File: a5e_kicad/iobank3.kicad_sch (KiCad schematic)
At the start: 3 parts, among them U7 A5EB013B-B23B

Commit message: add escape routing for channel A lpddr
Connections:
- net dq0: now also U7.M65 (3A_B_IO15_IOB_DIFF_IO_3A_B17n); no longer U7.AB62 (3A_B_IO12_IOB_DIFF_IO_3A_B18p)
- net dq1: now also U7.T51 (3A_B_IO22_IOB_DIFF_IO_3A_B13p); no longer U7.W62 (3A_B_IO13_IOB_DIFF_IO_3A_B18n)
- net dq5: now also U7.AB62 (3A_B_IO12_IOB_DIFF_IO_3A_B18p); no longer U7.M65 (3A_B_IO15_IOB_DIFF_IO_3A_B17n)
- net dq6: now also U7.W62 (3A_B_IO13_IOB_DIFF_IO_3A_B18n); no longer U7.T51 (3A_B_IO22_IOB_DIFF_IO_3A_B13p)
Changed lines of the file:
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@@
 		)
 	)
-	(label "dq6"
+	(label "dq1"
 		(at 208.28 104.14 0)
 		(effects
@@
 		)
 	)
-	(label "dq0"
+	(label "dq5"
 		(at 208.28 129.54 0)
 		(effects
@@
 		)
 	)
-	(label "dq5"
+	(label "dq0"
 		(at 208.28 121.92 0)
 		(effects
@@
 		)
 	)
-	(label "dq1"
+	(label "dq6"
 		(at 208.28 127 0)
 		(effects

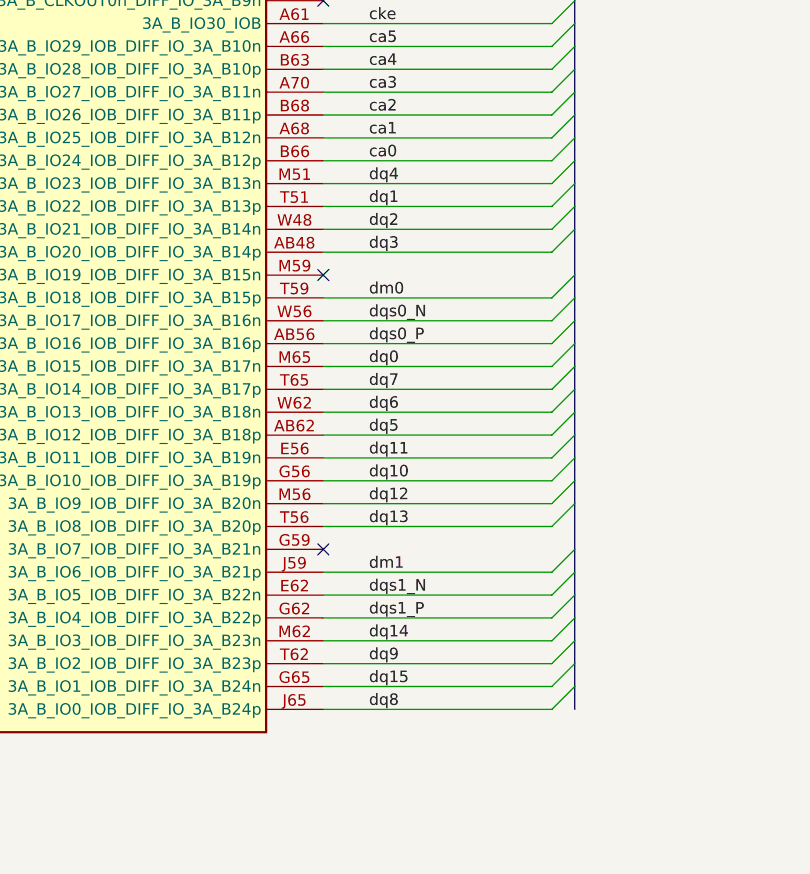
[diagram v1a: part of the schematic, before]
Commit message: iobank3: swap the channel A bytes (BL0 = byte 0, BL1 = byte 1)
Relabel the 22 U7-side labels of dq0-15, dqs0/1, dm0/1; each net keeps its
lane-pin position. Netlist: only the 22 channel A U7<->U12 pairs change.
BYTE_SWIZZLE_CH0=0 1 X X X X 3 2, PIN_SWIZZLE_CH0_DQS0=5 6 7 0 3 2 1 4
(DQS1-3 unchanged). The PCB is not updated yet: the routed dqs0/1 and dm0/1
on In2 end on the other byte's balls and need rerouting. In-lane pin swaps
follow by hand while routing.
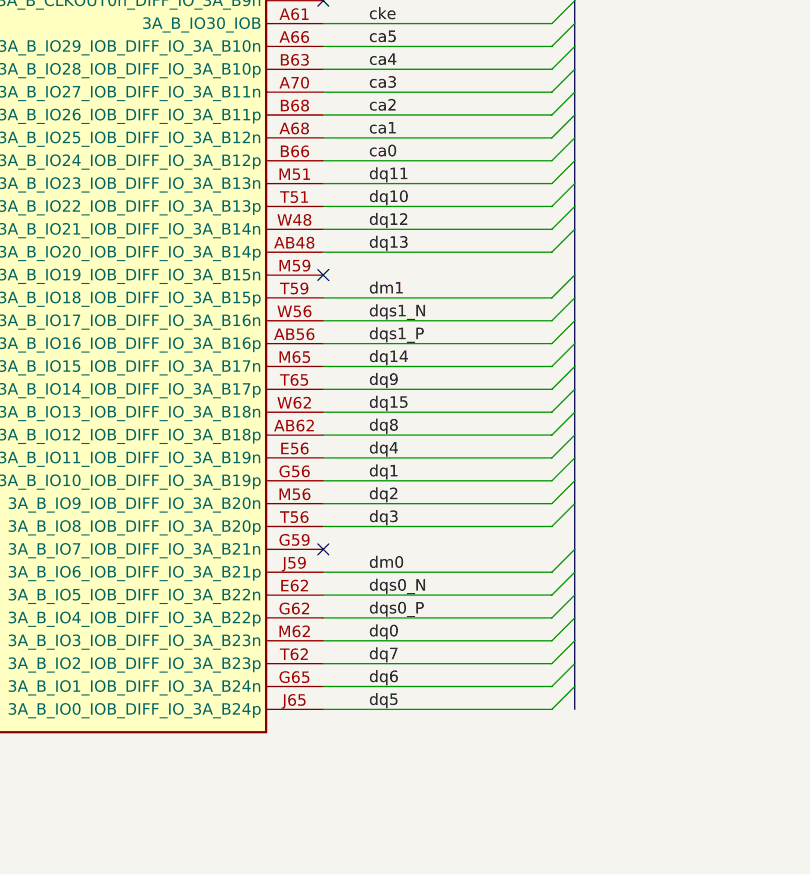
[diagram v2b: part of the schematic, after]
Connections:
- net dm0: now also U7.J59 (3A_B_IO6_IOB_DIFF_IO_3A_B21p); no longer U7.T59 (3A_B_IO18_IOB_DIFF_IO_3A_B15p)
- net dm1: now also U7.T59 (3A_B_IO18_IOB_DIFF_IO_3A_B15p); no longer U7.J59 (3A_B_IO6_IOB_DIFF_IO_3A_B21p)
- net dq0: now also U7.M62 (3A_B_IO3_IOB_DIFF_IO_3A_B23n); no longer U7.M65 (3A_B_IO15_IOB_DIFF_IO_3A_B17n)
- net dq1: now also U7.G56 (3A_B_IO10_IOB_DIFF_IO_3A_B19p); no longer U7.T51 (3A_B_IO22_IOB_DIFF_IO_3A_B13p)
- net dq10: now also U7.T51 (3A_B_IO22_IOB_DIFF_IO_3A_B13p); no longer U7.G56 (3A_B_IO10_IOB_DIFF_IO_3A_B19p)
- net dq11: now also U7.M51 (3A_B_IO23_IOB_DIFF_IO_3A_B13n); no longer U7.E56 (3A_B_IO11_IOB_DIFF_IO_3A_B19n)
- net dq12: now also U7.W48 (3A_B_IO21_IOB_DIFF_IO_3A_B14n); no longer U7.M56 (3A_B_IO9_IOB_DIFF_IO_3A_B20n)
- net dq13: now also U7.AB48 (3A_B_IO20_IOB_DIFF_IO_3A_B14p); no longer U7.T56 (3A_B_IO8_IOB_DIFF_IO_3A_B20p)
- net dq14: now also U7.M65 (3A_B_IO15_IOB_DIFF_IO_3A_B17n); no longer U7.M62 (3A_B_IO3_IOB_DIFF_IO_3A_B23n)
- net dq15: now also U7.W62 (3A_B_IO13_IOB_DIFF_IO_3A_B18n); no longer U7.G65 (3A_B_IO1_IOB_DIFF_IO_3A_B24n)
- net dq2: now also U7.M56 (3A_B_IO9_IOB_DIFF_IO_3A_B20n); no longer U7.W48 (3A_B_IO21_IOB_DIFF_IO_3A_B14n)
- net dq3: now also U7.T56 (3A_B_IO8_IOB_DIFF_IO_3A_B20p); no longer U7.AB48 (3A_B_IO20_IOB_DIFF_IO_3A_B14p)
- net dq4: now also U7.E56 (3A_B_IO11_IOB_DIFF_IO_3A_B19n); no longer U7.M51 (3A_B_IO23_IOB_DIFF_IO_3A_B13n)
- net dq5: now also U7.J65 (3A_B_IO0_IOB_DIFF_IO_3A_B24p); no longer U7.AB62 (3A_B_IO12_IOB_DIFF_IO_3A_B18p)
- net dq6: now also U7.G65 (3A_B_IO1_IOB_DIFF_IO_3A_B24n); no longer U7.W62 (3A_B_IO13_IOB_DIFF_IO_3A_B18n)
- net dq7: now also U7.T62 (3A_B_IO2_IOB_DIFF_IO_3A_B23p); no longer U7.T65 (3A_B_IO14_IOB_DIFF_IO_3A_B17p)
- net dq8: now also U7.AB62 (3A_B_IO12_IOB_DIFF_IO_3A_B18p); no longer U7.J65 (3A_B_IO0_IOB_DIFF_IO_3A_B24p)
- net dq9: now also U7.T65 (3A_B_IO14_IOB_DIFF_IO_3A_B17p); no longer U7.T62 (3A_B_IO2_IOB_DIFF_IO_3A_B23p)
- net dqs0_N: now also U7.E62 (3A_B_IO5_IOB_DIFF_IO_3A_B22n); no longer U7.W56 (3A_B_IO17_IOB_DIFF_IO_3A_B16n)
- net dqs0_P: now also U7.G62 (3A_B_IO4_IOB_DIFF_IO_3A_B22p); no longer U7.AB56 (3A_B_IO16_IOB_DIFF_IO_3A_B16p)
- net dqs1_N: now also U7.W56 (3A_B_IO17_IOB_DIFF_IO_3A_B16n); no longer U7.E62 (3A_B_IO5_IOB_DIFF_IO_3A_B22n)
- net dqs1_P: now also U7.AB56 (3A_B_IO16_IOB_DIFF_IO_3A_B16p); no longer U7.G62 (3A_B_IO4_IOB_DIFF_IO_3A_B22p)
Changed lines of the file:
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@@
 		)
 	)
-	(label "dqs0_N"
+	(label "dqs1_N"
 		(at 208.28 116.84 0)
 		(effects
@@
 		)
 	)
-	(label "dq7"
+	(label "dq9"
 		(at 208.28 124.46 0)
 		(effects
@@
 		)
 	)
-	(label "dq1"
+	(label "dq10"
 		(at 208.28 104.14 0)
 		(effects
@@
 		)
 	)
-	(label "dq5"
+	(label "dq8"
 		(at 208.28 129.54 0)
 		(effects
@@
 		)
 	)
-	(label "dm1"
+	(label "dm0"
 		(at 208.28 144.78 0)
 		(effects
@@
 		)
 	)
-	(label "dq12"
+	(label "dq2"
 		(at 208.28 137.16 0)
 		(effects
@@
 		)
 	)
-	(label "dq3"
+	(label "dq13"
 		(at 208.28 109.22 0)
 		(effects
@@
 		)
 	)
-	(label "dq8"
+	(label "dq5"
 		(at 208.28 160.02 0)
 		(effects
@@
 		)
 	)
+	(label "dq4"
+		(at 208.28 132.08 0)
+		(effects
+			(font
+				(size 1.27 1.27)
+			)
+			(justify left bottom)
+		)
+	)
 	(label "dq11"
-		(at 208.28 132.08 0)
-		(effects
-			(font
-				(size 1.27 1.27)
-			)
-			(justify left bottom)
-		)
-	)
-	(label "dq4"
 		(at 208.28 101.6 0)
 		(effects
@@
 		)
 	)
-	(label "dq9"
+	(label "dq7"
 		(at 208.28 154.94 0)
 		(effects
@@
 		)
 	)
-	(label "dqs1_P"
+	(label "dqs0_P"
 		(at 208.28 149.86 0)
 		(effects
@@
 		)
 	)
-	(label "dq15"
+	(label "dq6"
 		(at 208.28 157.48 0)
 		(effects
@@
 		)
 	)
-	(label "dq14"
+	(label "dq0"
 		(at 208.28 152.4 0)
 		(effects
@@
 		)
 	)
-	(label "dq0"
+	(label "dq14"
 		(at 208.28 121.92 0)
 		(effects
@@
 		)
 	)
-	(label "dq13"
+	(label "dq3"
 		(at 208.28 139.7 0)
 		(effects
@@
 		)
 	)
-	(label "dq10"
+	(label "dq1"
 		(at 208.28 134.62 0)
 		(effects
@@
 		)
 	)
-	(label "dm0"
+	(label "dm1"
 		(at 208.28 114.3 0)
 		(effects
@@
 		)
 	)
-	(label "dqs0_P"
+	(label "dqs1_P"
 		(at 208.28 119.38 0)
 		(effects
@@
 		)
 	)
-	(label "dq2"
+	(label "dq12"
 		(at 208.28 106.68 0)
 		(effects
@@
 		)
 	)
-	(label "dq6"
+	(label "dq15"
 		(at 208.28 127 0)
 		(effects
@@
 		)
 	)
-	(label "dqs1_N"
+	(label "dqs0_N"
 		(at 208.28 147.32 0)
 		(effects

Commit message: route lpddr4 io
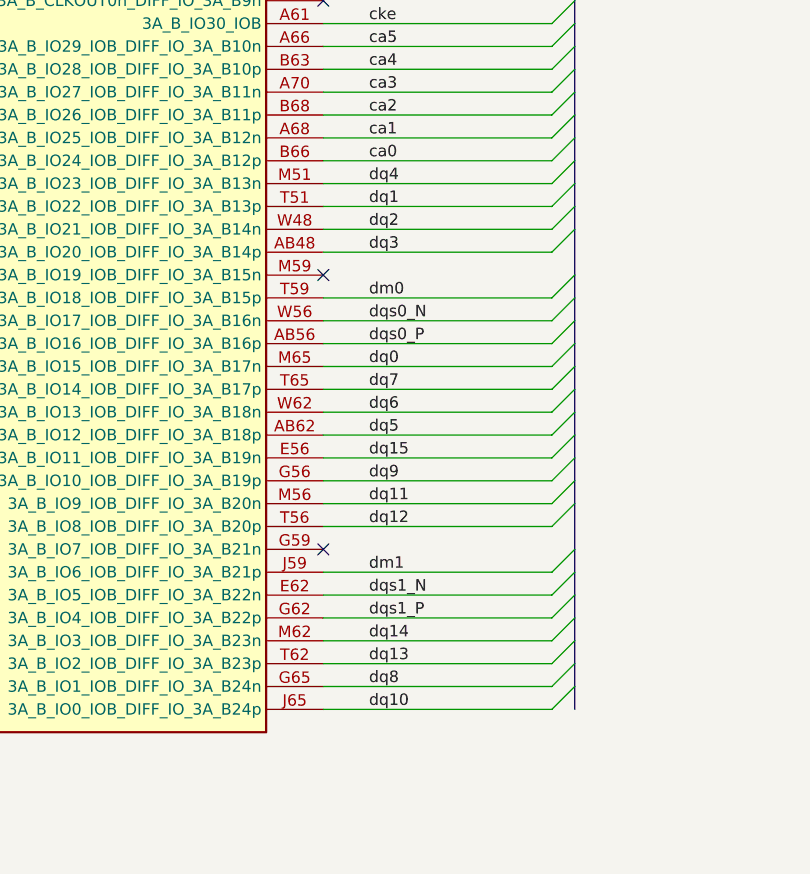
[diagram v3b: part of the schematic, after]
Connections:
- net dm0: now also U7.T59 (3A_B_IO18_IOB_DIFF_IO_3A_B15p); no longer U7.J59 (3A_B_IO6_IOB_DIFF_IO_3A_B21p)
- net dm1: now also U7.J59 (3A_B_IO6_IOB_DIFF_IO_3A_B21p); no longer U7.T59 (3A_B_IO18_IOB_DIFF_IO_3A_B15p)
- net dq0: now also U7.M65 (3A_B_IO15_IOB_DIFF_IO_3A_B17n); no longer U7.M62 (3A_B_IO3_IOB_DIFF_IO_3A_B23n)
- net dq1: now also U7.T51 (3A_B_IO22_IOB_DIFF_IO_3A_B13p); no longer U7.G56 (3A_B_IO10_IOB_DIFF_IO_3A_B19p)
- net dq10: now also U7.J65 (3A_B_IO0_IOB_DIFF_IO_3A_B24p); no longer U7.T51 (3A_B_IO22_IOB_DIFF_IO_3A_B13p)
- net dq11: now also U7.M56 (3A_B_IO9_IOB_DIFF_IO_3A_B20n); no longer U7.M51 (3A_B_IO23_IOB_DIFF_IO_3A_B13n)
- net dq12: now also U7.T56 (3A_B_IO8_IOB_DIFF_IO_3A_B20p); no longer U7.W48 (3A_B_IO21_IOB_DIFF_IO_3A_B14n)
- net dq13: now also U7.T62 (3A_B_IO2_IOB_DIFF_IO_3A_B23p); no longer U7.AB48 (3A_B_IO20_IOB_DIFF_IO_3A_B14p)
- net dq14: now also U7.M62 (3A_B_IO3_IOB_DIFF_IO_3A_B23n); no longer U7.M65 (3A_B_IO15_IOB_DIFF_IO_3A_B17n)
- net dq15: now also U7.E56 (3A_B_IO11_IOB_DIFF_IO_3A_B19n); no longer U7.W62 (3A_B_IO13_IOB_DIFF_IO_3A_B18n)
- net dq2: now also U7.W48 (3A_B_IO21_IOB_DIFF_IO_3A_B14n); no longer U7.M56 (3A_B_IO9_IOB_DIFF_IO_3A_B20n)
- net dq3: now also U7.AB48 (3A_B_IO20_IOB_DIFF_IO_3A_B14p); no longer U7.T56 (3A_B_IO8_IOB_DIFF_IO_3A_B20p)
- net dq4: now also U7.M51 (3A_B_IO23_IOB_DIFF_IO_3A_B13n); no longer U7.E56 (3A_B_IO11_IOB_DIFF_IO_3A_B19n)
- net dq5: now also U7.AB62 (3A_B_IO12_IOB_DIFF_IO_3A_B18p); no longer U7.J65 (3A_B_IO0_IOB_DIFF_IO_3A_B24p)
- net dq6: now also U7.W62 (3A_B_IO13_IOB_DIFF_IO_3A_B18n); no longer U7.G65 (3A_B_IO1_IOB_DIFF_IO_3A_B24n)
- net dq7: now also U7.T65 (3A_B_IO14_IOB_DIFF_IO_3A_B17p); no longer U7.T62 (3A_B_IO2_IOB_DIFF_IO_3A_B23p)
- net dq8: now also U7.G65 (3A_B_IO1_IOB_DIFF_IO_3A_B24n); no longer U7.AB62 (3A_B_IO12_IOB_DIFF_IO_3A_B18p)
- net dq9: now also U7.G56 (3A_B_IO10_IOB_DIFF_IO_3A_B19p); no longer U7.T65 (3A_B_IO14_IOB_DIFF_IO_3A_B17p)
- net dqs0_N: now also U7.W56 (3A_B_IO17_IOB_DIFF_IO_3A_B16n); no longer U7.E62 (3A_B_IO5_IOB_DIFF_IO_3A_B22n)
- net dqs0_P: now also U7.AB56 (3A_B_IO16_IOB_DIFF_IO_3A_B16p); no longer U7.G62 (3A_B_IO4_IOB_DIFF_IO_3A_B22p)
- net dqs1_N: now also U7.E62 (3A_B_IO5_IOB_DIFF_IO_3A_B22n); no longer U7.W56 (3A_B_IO17_IOB_DIFF_IO_3A_B16n)
- net dqs1_P: now also U7.G62 (3A_B_IO4_IOB_DIFF_IO_3A_B22p); no longer U7.AB56 (3A_B_IO16_IOB_DIFF_IO_3A_B16p)
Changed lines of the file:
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@@
 		)
 	)
-	(label "dqs1_N"
+	(label "dqs0_N"
 		(at 208.28 116.84 0)
 		(effects
@@
 		)
 	)
-	(label "dq9"
+	(label "dq7"
 		(at 208.28 124.46 0)
 		(effects
@@
 		)
 	)
-	(label "dq10"
+	(label "dq1"
 		(at 208.28 104.14 0)
 		(effects
@@
 		)
 	)
-	(label "dq8"
+	(label "dq5"
 		(at 208.28 129.54 0)
 		(effects
@@
 		)
 	)
-	(label "dm0"
+	(label "dm1"
 		(at 208.28 144.78 0)
 		(effects
@@
 		)
 	)
-	(label "dq2"
+	(label "dq11"
 		(at 208.28 137.16 0)
 		(effects
@@
 		)
 	)
+	(label "dq3"
+		(at 208.28 109.22 0)
+		(effects
+			(font
+				(size 1.27 1.27)
+			)
+			(justify left bottom)
+		)
+	)
+	(label "dq10"
+		(at 208.28 160.02 0)
+		(effects
+			(font
+				(size 1.27 1.27)
+			)
+			(justify left bottom)
+		)
+	)
+	(label "dq15"
+		(at 208.28 132.08 0)
+		(effects
+			(font
+				(size 1.27 1.27)
+			)
+			(justify left bottom)
+		)
+	)
+	(label "dq4"
+		(at 208.28 101.6 0)
+		(effects
+			(font
+				(size 1.27 1.27)
+			)
+			(justify left bottom)
+		)
+	)
 	(label "dq13"
-		(at 208.28 109.22 0)
-		(effects
-			(font
-				(size 1.27 1.27)
-			)
-			(justify left bottom)
-		)
-	)
-	(label "dq5"
-		(at 208.28 160.02 0)
-		(effects
-			(font
-				(size 1.27 1.27)
-			)
-			(justify left bottom)
-		)
-	)
-	(label "dq4"
-		(at 208.28 132.08 0)
-		(effects
-			(font
-				(size 1.27 1.27)
-			)
-			(justify left bottom)
-		)
-	)
-	(label "dq11"
-		(at 208.28 101.6 0)
-		(effects
-			(font
-				(size 1.27 1.27)
-			)
-			(justify left bottom)
-		)
-	)
-	(label "dq7"
 		(at 208.28 154.94 0)
 		(effects
@@
 		)
 	)
-	(label "dqs0_P"
+	(label "dqs1_P"
 		(at 208.28 149.86 0)
 		(effects
@@
 		)
 	)
-	(label "dq6"
+	(label "dq8"
 		(at 208.28 157.48 0)
 		(effects
@@
 		)
 	)
-	(label "dq0"
+	(label "dq14"
 		(at 208.28 152.4 0)
 		(effects
@@
 		)
 	)
-	(label "dq14"
+	(label "dq0"
 		(at 208.28 121.92 0)
 		(effects
@@
 		)
 	)
-	(label "dq3"
+	(label "dq12"
 		(at 208.28 139.7 0)
 		(effects
@@
 		)
 	)
-	(label "dq1"
+	(label "dq9"
 		(at 208.28 134.62 0)
 		(effects
@@
 		)
 	)
-	(label "dm1"
+	(label "dm0"
 		(at 208.28 114.3 0)
 		(effects
@@
 		)
 	)
-	(label "dqs1_P"
+	(label "dqs0_P"
 		(at 208.28 119.38 0)
 		(effects
@@
 		)
 	)
-	(label "dq12"
+	(label "dq2"
 		(at 208.28 106.68 0)
 		(effects
@@
 		)
 	)
-	(label "dq15"
+	(label "dq6"
 		(at 208.28 127 0)
 		(effects
@@
 		)
 	)
-	(label "dqs0_N"
+	(label "dqs1_N"
 		(at 208.28 147.32 0)
 		(effects

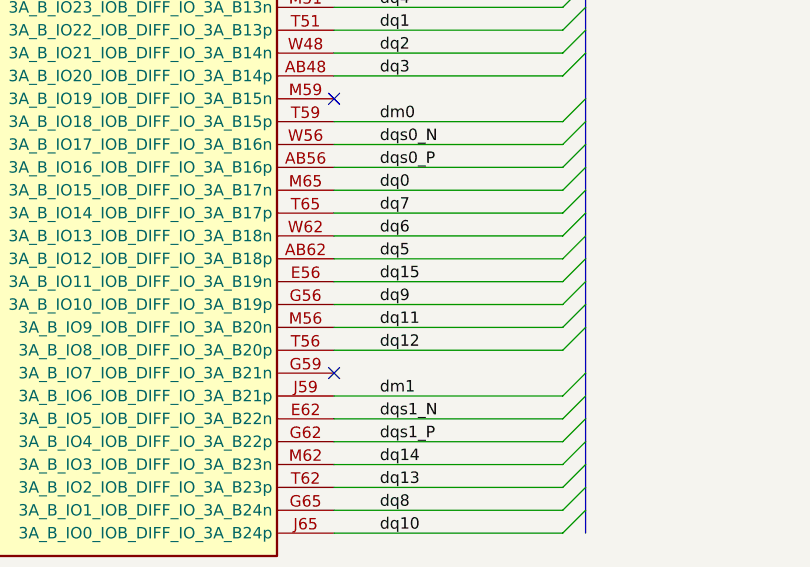
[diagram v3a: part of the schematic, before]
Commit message: match delays in L5
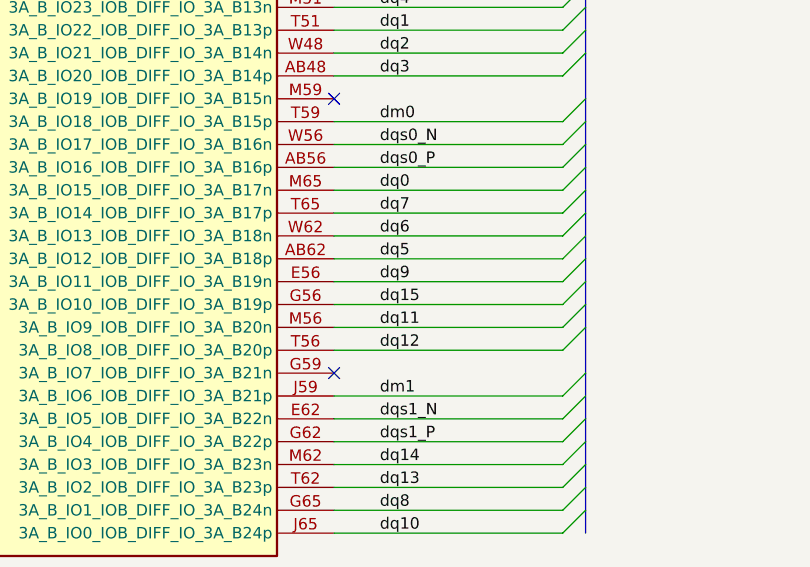
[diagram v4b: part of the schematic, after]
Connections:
- net dq15: now also U7.G56 (3A_B_IO10_IOB_DIFF_IO_3A_B19p); no longer U7.E56 (3A_B_IO11_IOB_DIFF_IO_3A_B19n)
- net dq9: now also U7.E56 (3A_B_IO11_IOB_DIFF_IO_3A_B19n); no longer U7.G56 (3A_B_IO10_IOB_DIFF_IO_3A_B19p)
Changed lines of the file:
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@@
 		)
 	)
-	(label "dq15"
+	(label "dq9"
 		(at 208.28 132.08 0)
 		(effects
@@
 		)
 	)
-	(label "dq9"
+	(label "dq15"
 		(at 208.28 134.62 0)
 		(effects

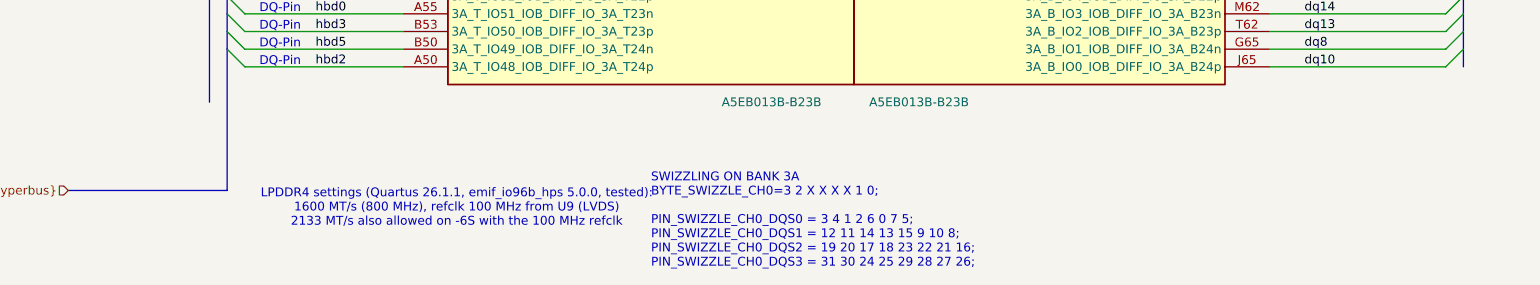
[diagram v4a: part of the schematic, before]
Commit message: Schematic reorg step 1: remove dangling stubs and stale notes, correct notes, fill title blocks
Netlist: 0 renamed, 0 connectivity diffs; DRC parity 0. ERC 315 -> 242.
Plan refreshed for the eMMC, RTL8211FDI, TPS548A28 and the tuned LPDDR4 (IOBANK 3 sheet name kept).
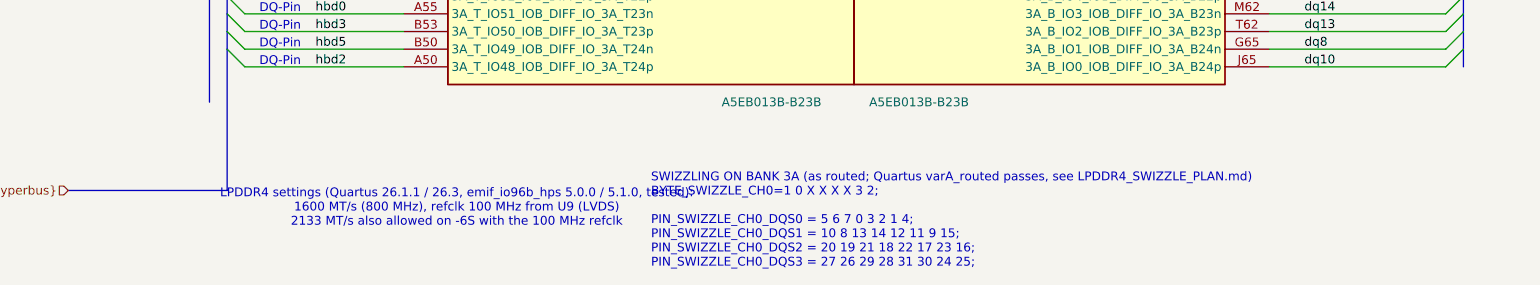
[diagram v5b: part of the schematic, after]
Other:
- note added: "LPDDR4 settings (Quartus 26.1.1 / 26.3, emif_io96b_hps 5.0.0 / 5.1.0, tested): 1600 MT/s (800 MHz), refclk 100 MHz from U9 (LVDS) 2133 MT/s also allowed on -6S with the 100 MHz refclk"
- note added: "SWIZZLING ON BANK 3A (as routed; Quartus varA_routed passes, see LPDDR4_SWIZZLE_PLAN.md) BYTE_SWIZZLE_CH0=1 0 X X X X 3 2; PIN_SWIZZLE_CH0_DQS0 = 5 6 7 0 3 2 1 4; PIN_SWIZZLE_CH0_DQS1 = 10 8 13 14 12 11 9 15; PIN_SWIZZLE_CH0_DQS2 = 20 19 21 18 22 17 23 16; PIN_SWIZZLE_CH0_DQS3 = 27 26 29 28 31 30 24 25;"
- note removed: "LPDDR4 settings (Quartus 26.1.1, emif_io96b_hps 5.0.0, tested): 1600 MT/s (800 MHz), refclk 100 MHz from U9 (LVDS) 2133 MT/s also allowed on -6S with the 100 MHz refclk"
- note removed: "SWIZZLING ON BANK 3A BYTE_SWIZZLE_CH0=3 2 X X X X 1 0; PIN_SWIZZLE_CH0_DQS0 = 3 4 1 2 6 0 7 5; PIN_SWIZZLE_CH0_DQS1 = 12 11 14 13 15 9 10 8; PIN_SWIZZLE_CH0_DQS2 = 19 20 17 18 23 22 21 16; PIN_SWIZZLE_CH0_DQS3 = 31 30 24 25 29 28 27 26;"
- title: (none) -> Bank 3A: LPDDR4 controller
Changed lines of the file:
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@@
 	(paper "A4")
 	(title_block
-		(rev "0.1")
+		(title "Bank 3A: LPDDR4 controller")
+		(rev "${REVISION}")
+		(comment 1 "${BOARD}")
 	)
 	(text "DQS-Pin"
@@
 		)
 	)
-	(text "SWIZZLING ON BANK 3A\nBYTE_SWIZZLE_CH0=3 2 X X X X 1 0;\n\nPIN_SWIZZLE_CH0_DQS0 = 3 4 1 2 6 0 7 5;\nPIN_SWIZZLE_CH0_DQS1 = 12 11 14 13 15 9 10 8;\nPIN_SWIZZLE_CH0_DQS2 = 19 20 17 18 23 22 21 16;\nPIN_SWIZZLE_CH0_DQS3 = 31 30 24 25 29 28 27 26;"
+	(text "SWIZZLING ON BANK 3A (as routed; Quartus varA_routed passes, see LPDDR4_SWIZZLE_PLAN.md)\nBYTE_SWIZZLE_CH0=1 0 X X X X 3 2;\n\nPIN_SWIZZLE_CH0_DQS0 = 5 6 7 0 3 2 1 4;\nPIN_SWIZZLE_CH0_DQS1 = 10 8 13 14 12 11 9 15;\nPIN_SWIZZLE_CH0_DQS2 = 20 19 21 18 22 17 23 16;\nPIN_SWIZZLE_CH0_DQS3 = 27 26 29 28 31 30 24 25;"
 		(exclude_from_sim no)
 		(at 114.3 175.26 0)
@@
 		)
 	)
-	(text "LPDDR4 settings (Quartus 26.1.1, emif_io96b_hps 5.0.0, tested):\n1600 MT/s (800 MHz), refclk 100 MHz from U9 (LVDS)\n2133 MT/s also allowed on -6S with the 100 MHz refclk"
+	(text "LPDDR4 settings (Quartus 26.1.1 / 26.3, emif_io96b_hps 5.0.0 / 5.1.0, tested):\n1600 MT/s (800 MHz), refclk 100 MHz from U9 (LVDS)\n2133 MT/s also allowed on -6S with the 100 MHz refclk"
 		(exclude_from_sim no)
 		(at 86.36 180.34 0)
